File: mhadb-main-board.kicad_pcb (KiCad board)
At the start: 4 copper layers, 50 x 50 mm, 109 parts, among them J1 Conn_01x04, J10 Conn_01x04_Pin, J2 Conn_01x04, J3 USB_C_Receptacle_USB2.0_14P, J4 Conn_01x02, J5 Conn_01x03, J6 Conn_01x03, J7 Conn_01x04, J8 Conn_01x04, J9 Conn_01x02_Pin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

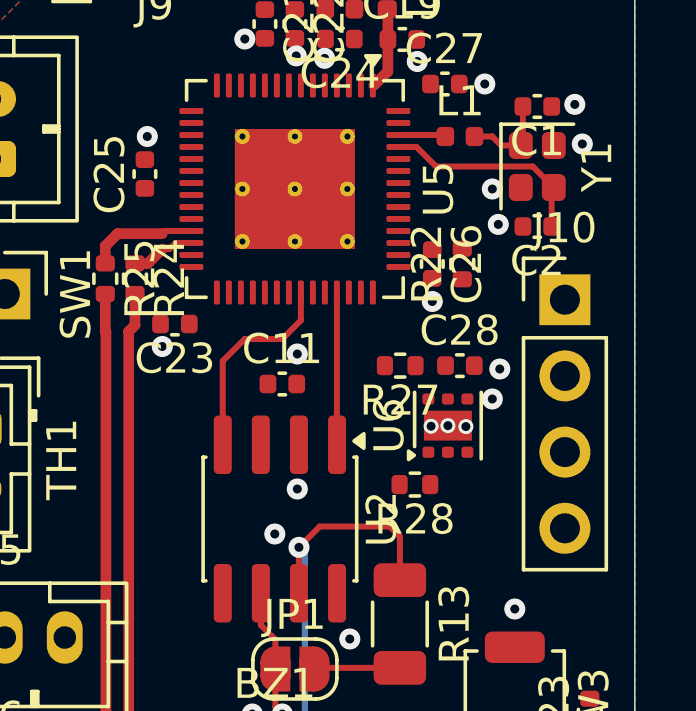
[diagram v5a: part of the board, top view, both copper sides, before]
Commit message: pcb: add UART routing
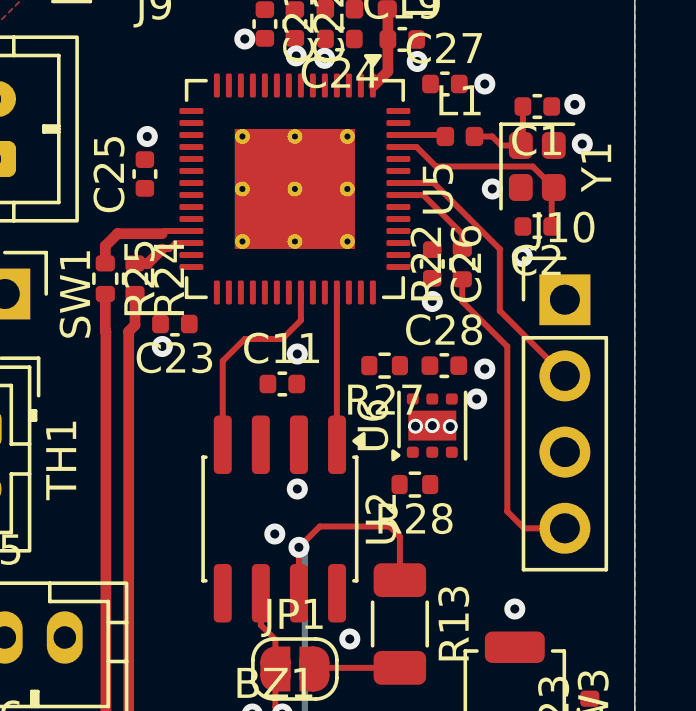
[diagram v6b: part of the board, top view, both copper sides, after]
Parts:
- moved R27 0.52 mm to (145.7, 69.4)
- moved U6 0.52 mm to (147.2, 71.4)
- moved C28 0.52 mm to (147.7, 69.4)
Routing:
- net Net-(J10-Pin_4): track 0.00 -> 10.5 mm
- net /U0RXD: track 0.00 -> 9.42 mm
- net /U0TXD: track 0.00 -> 3.16 mm
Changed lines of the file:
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@@
 	(footprint "Resistor_SMD:R_0402_1005Metric"
 		(layer "F.Cu")
-		(at 146.18 69.3875 180)
+		(at 145.66 69.3875 180)
 		(descr "Resistor SMD 0402 (1005 Metric), square (rectangular) end terminal, IPC-7351 nominal, (Body size source: IPC-SM-782 page 72, https://www.pcb-3d.com/wordpress/wp-content/uploads/ipc-sm-782a_amendment_1_and_2.pdf), generated with kicad-footprint-generator")
 		(tags "resistor")
@@
 	(footprint "Capacitor_SMD:C_0402_1005Metric"
 		(layer "F.Cu")
-		(at 148.17 69.3875)
+		(at 147.65 69.3875)
 		(descr "Capacitor SMD 0402 (1005 Metric), square (rectangular) end terminal, IPC-7351 nominal, (Body size source: IPC-SM-782 page 76, https://www.pcb-3d.com/wordpress/wp-content/uploads/ipc-sm-782a_amendment_1_and_2.pdf), generated with kicad-footprint-generator")
 		(tags "capacitor")
@@
 	(footprint "Package_SON:WSON-6-1EP_2x2mm_P0.65mm_EP1x1.6mm"
 		(layer "F.Cu")
-		(at 147.77 71.3875 90)
+		(at 147.25 71.3875 90)
 		(descr "WSON, 6 Pin (http://www.ti.com/lit/ds/symlink/tps61040.pdf#page=35), generated with kicad-footprint-generator ipc_noLead_generator.py")
 		(tags "WSON NoLead")
@@
 	)
 	(via
-		(at 149.25 70.5)
+		(at 148.73 70.5)
 		(size 0.7)
 		(drill 0.3)
@@
 	)
 	(via
-		(at 149.45 64.68)
+		(at 150.25 65.75)
 		(size 0.7)
 		(drill 0.3)
@@
 	)
 	(via
-		(at 147.77 71.3875)
+		(at 147.25 71.3875)
 		(size 0.5)
 		(drill 0.3)
@@
 	)
 	(via
-		(at 148.369638 71.418936)
+		(at 147.849638 71.418936)
 		(size 0.5)
 		(drill 0.3)
@@
 	)
 	(via
-		(at 147.210245 71.406922)
+		(at 146.690245 71.406922)
 		(size 0.5)
 		(drill 0.3)
@@
 	)
 	(via
-		(at 149.5 69.5)
+		(at 149 69.5)
 		(size 0.7)
 		(drill 0.3)
@@
 	)
 	(segment
+		(start 150.31 74.81)
+		(end 151.67 74.81)
+		(width 0.2)
+		(layer "F.Cu")
+		(net 40)
+	)
+	(segment
+		(start 149.75 74.25)
+		(end 150.31 74.81)
+		(width 0.2)
+		(layer "F.Cu")
+		(net 40)
+	)
+	(segment
+		(start 149.75 68.75)
+		(end 149.75 74.25)
+		(width 0.2)
+		(layer "F.Cu")
+		(net 40)
+	)
+	(segment
+		(start 148.25 66.51)
+		(end 148.25 67.25)
+		(width 0.2)
+		(layer "F.Cu")
+		(net 40)
+	)
+	(segment
+		(start 148.25 67.25)
+		(end 149.75 68.75)
+		(width 0.2)
+		(layer "F.Cu")
+		(net 40)
+	)
+	(segment
+		(start 146.12 63.3)
+		(end 147.3 63.3)
+		(width 0.2)
+		(layer "F.Cu")
+		(net 41)
+	)
+	(segment
+		(start 149.5 65.5)
+		(end 149.5 67.56)
+		(width 0.2)
+		(layer "F.Cu")
+		(net 41)
+	)
+	(segment
+		(start 147.3 63.3)
+		(end 149.5 65.5)
+		(width 0.2)
+		(layer "F.Cu")
+		(net 41)
+	)
+	(segment
+		(start 149.5 67.56)
+		(end 151.67 69.73)
+		(width 0.2)
+		(layer "F.Cu")
+		(net 41)
+	)
+	(segment
 		(start 146.17 79.4625)
 		(end 143.3575 79.4625)
@@
 	)
 	(segment
+		(start 148.25 65)
+		(end 146.95 63.7)
+		(width 0.2)
+		(layer "F.Cu")
+		(net 56)
+	)
+	(segment
+		(start 146.95 63.7)
+		(end 146.12 63.7)
+		(width 0.2)
+		(layer "F.Cu")
+		(net 56)
+	)
+	(segment
+		(start 148.25 65.49)
+		(end 148.25 65)
+		(width 0.2)
+		(layer "F.Cu")
+		(net 56)
+	)
+	(segment

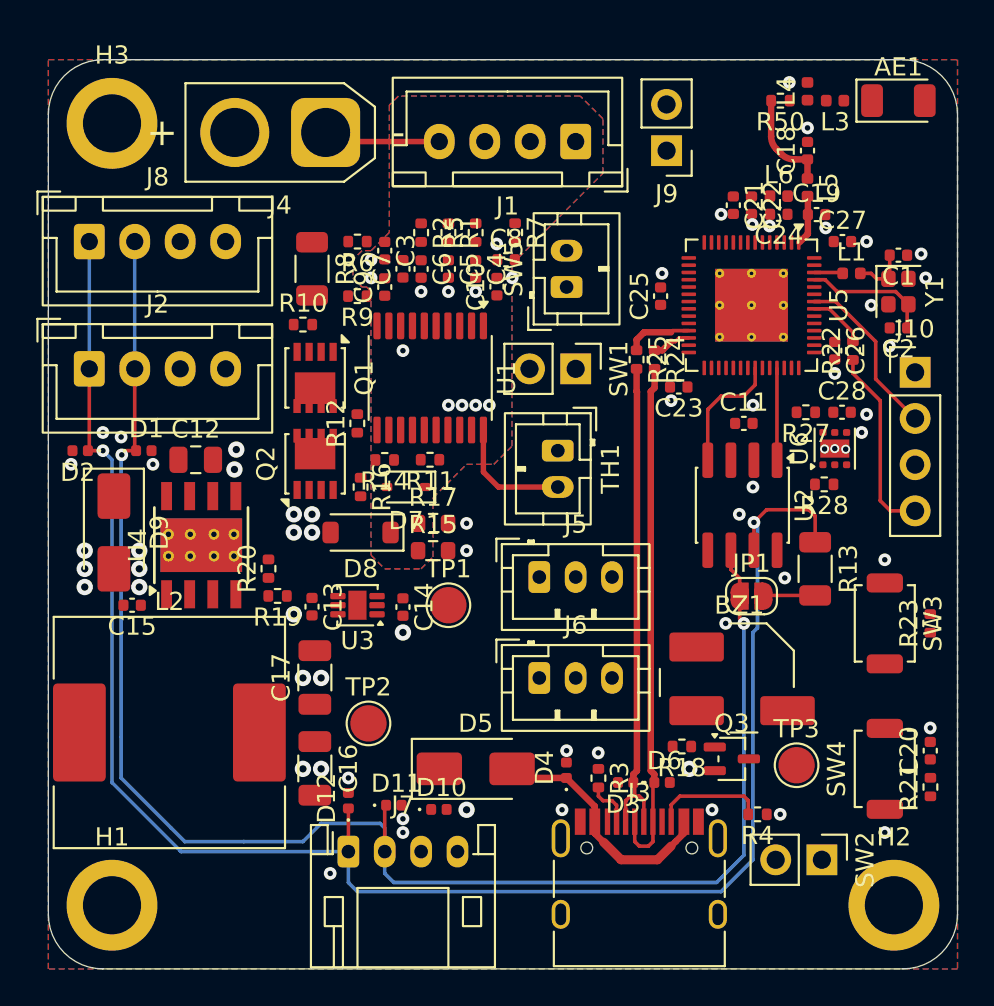
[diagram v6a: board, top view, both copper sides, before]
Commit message: pcb: add SMPS routing
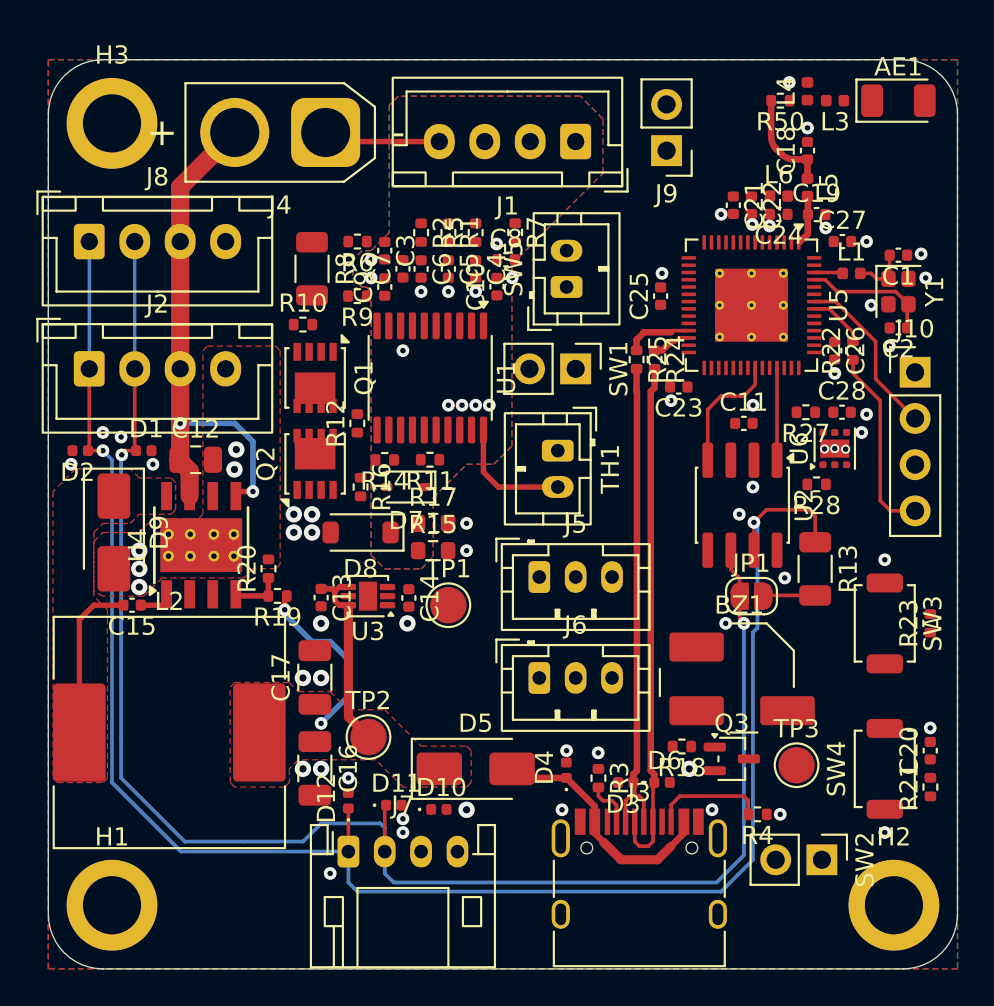
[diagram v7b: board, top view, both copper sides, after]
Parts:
- moved U3 0.76 mm to (121.6, 79.5)
- moved TP2 0.75 mm to (121.6, 87.2)
- moved C13 0.71 mm to (119.0, 79.6)
- moved C14 0.60 mm to (123.8, 79.6)
- moved R28 0.42 mm to (146.2, 73.4)
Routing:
- net +BATT: track 0.00 -> 29.7 mm, vias 0 -> 2
- net +5V: track 0.00 -> 20.4 mm, vias 0 -> 2
- net Net-(D9-K): track 0.00 -> 8.95 mm
- net Net-(U4-VSENSE): track 0.00 -> 2.82 mm
- net Net-(U4-BOOT): track 0.00 -> 2.02 mm
- net GND: vias 62 -> 59
- added copper zone on F.Cu, net +5V
- added copper zone on F.Cu, net Net-(D9-K)

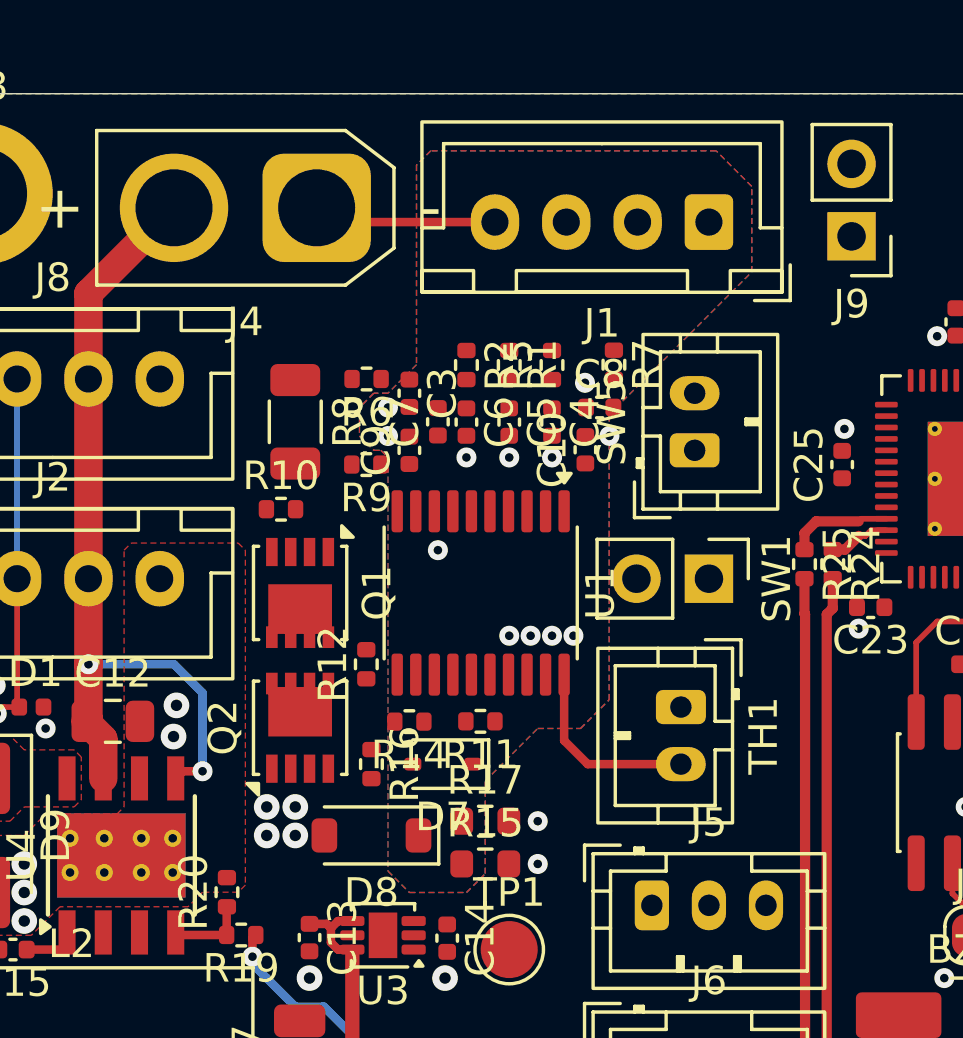
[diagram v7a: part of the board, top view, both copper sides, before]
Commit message: pcb: add BQ77905 Battery protection routing
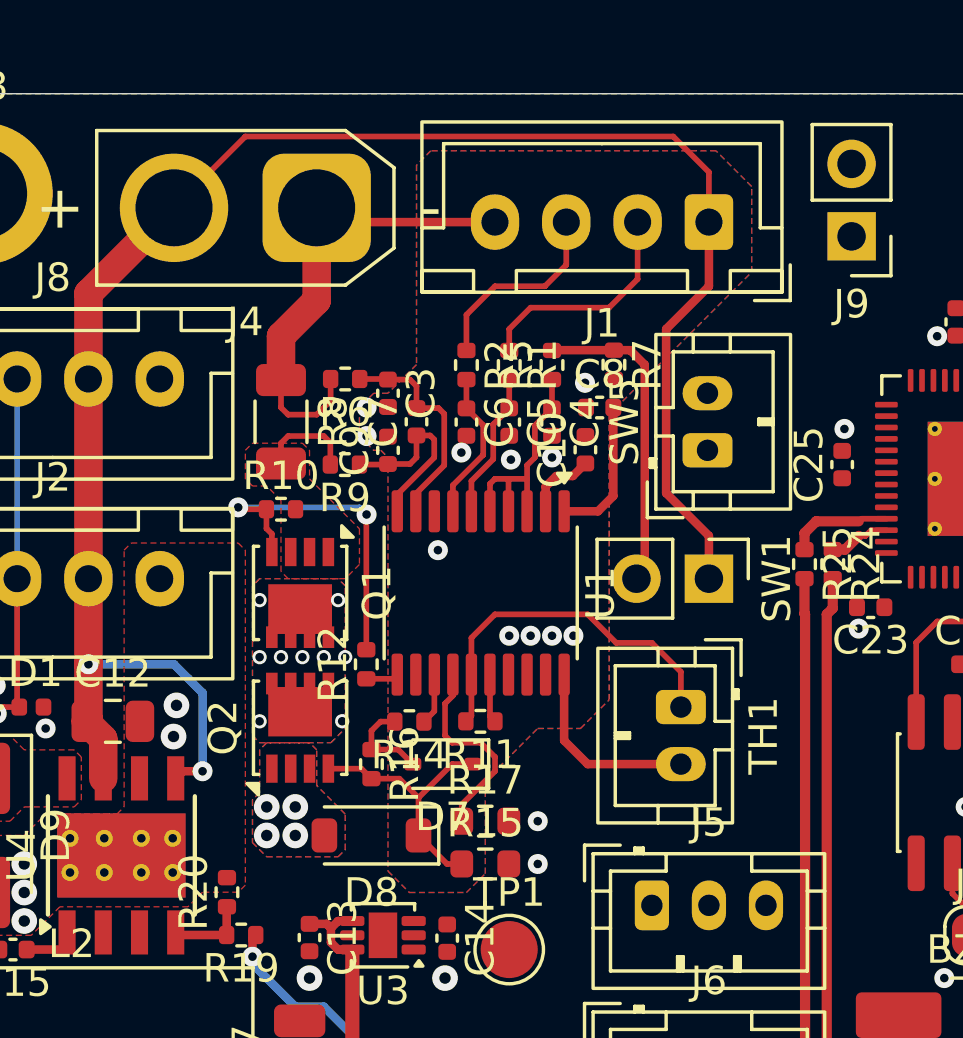
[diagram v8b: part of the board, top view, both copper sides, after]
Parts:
- moved C3 0.75 mm to (121.8, 60.5)
- moved C7 0.75 mm to (122.8, 61.5)
- moved C9 0.75 mm to (121.8, 62.5)
- moved R6 0.75 mm to (120.2, 60.0)
- moved R9 0.75 mm to (120.2, 63.0)
- moved R8 0.50 mm to (118.0, 61.5)
- moved SW5 0.45 mm to (132.9, 62.5)
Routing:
- net +BATT: track 29.7 -> 65.5 mm
- net Net-(U1-TS): track 0.00 -> 12.8 mm
- net Net-(Q1-G): track 0.00 -> 11.9 mm, vias 0 -> 2
- net Net-(SW1-B): track 0.00 -> 11.1 mm
- net BGND: track 13.2 -> 23.5 mm
- net Net-(D7-K): track 0.00 -> 9.22 mm
- net Net-(U1-VC3): track 0.00 -> 8.46 mm
- net Net-(J1-Pin_2): track 0.00 -> 7.97 mm
- net Net-(U1-SRP): track 0.00 -> 7.75 mm
- net Net-(U1-LD): track 0.00 -> 7.04 mm
- net Net-(J1-Pin_3): track 0.00 -> 6.97 mm
- net Net-(U1-SRN): track 0.00 -> 6.61 mm
- net Net-(U1-VC1): track 0.00 -> 5.30 mm
- net Net-(U1-VC2): track 0.00 -> 5.20 mm
- net Net-(U1-VDD): track 0.00 -> 5.05 mm
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- added copper zone on B.Cu, net Net-(Q1-D)
- added copper zone on F.Cu, net Net-(Q1-D)
- added copper zone on F.Cu, net Net-(Q1-S-Pad1)
